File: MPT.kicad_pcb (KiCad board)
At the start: 2 copper layers, 60 x 50 mm, 55 parts, among them J1 USB4105GFA120, J2 ER-TFT2.79-1, Q1 BSS138, SW1 OS102011MA1QN1, SW2 KMR421GULCLFS, SW3 KMR421GULCLFS, U1 TPS62590, U2 BQ25185, U3 BQ27441-G1, U4 ESP32-S3-WROOM-1-N4R2, U5 RCLAMP0854P.TCT

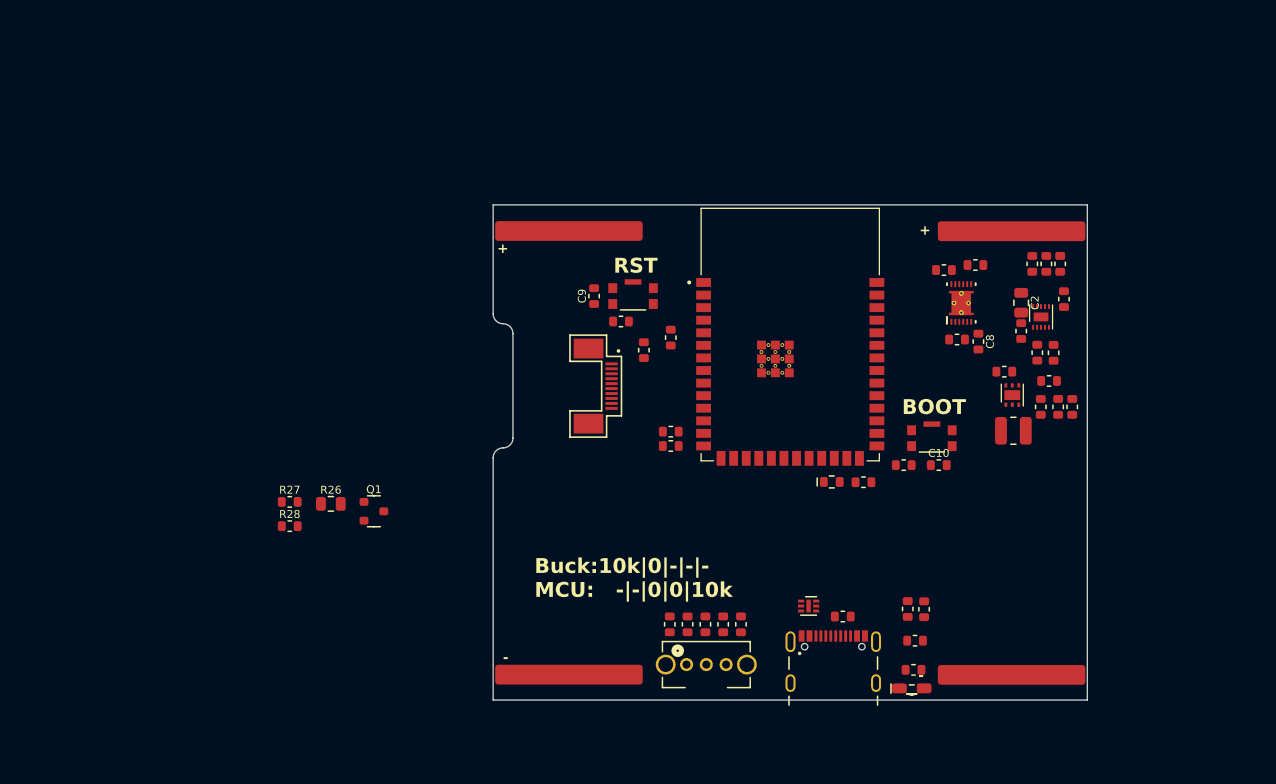
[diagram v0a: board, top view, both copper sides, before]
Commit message: Updated PCB Layout with new Buck Boost, Display driver and STAT Led logic
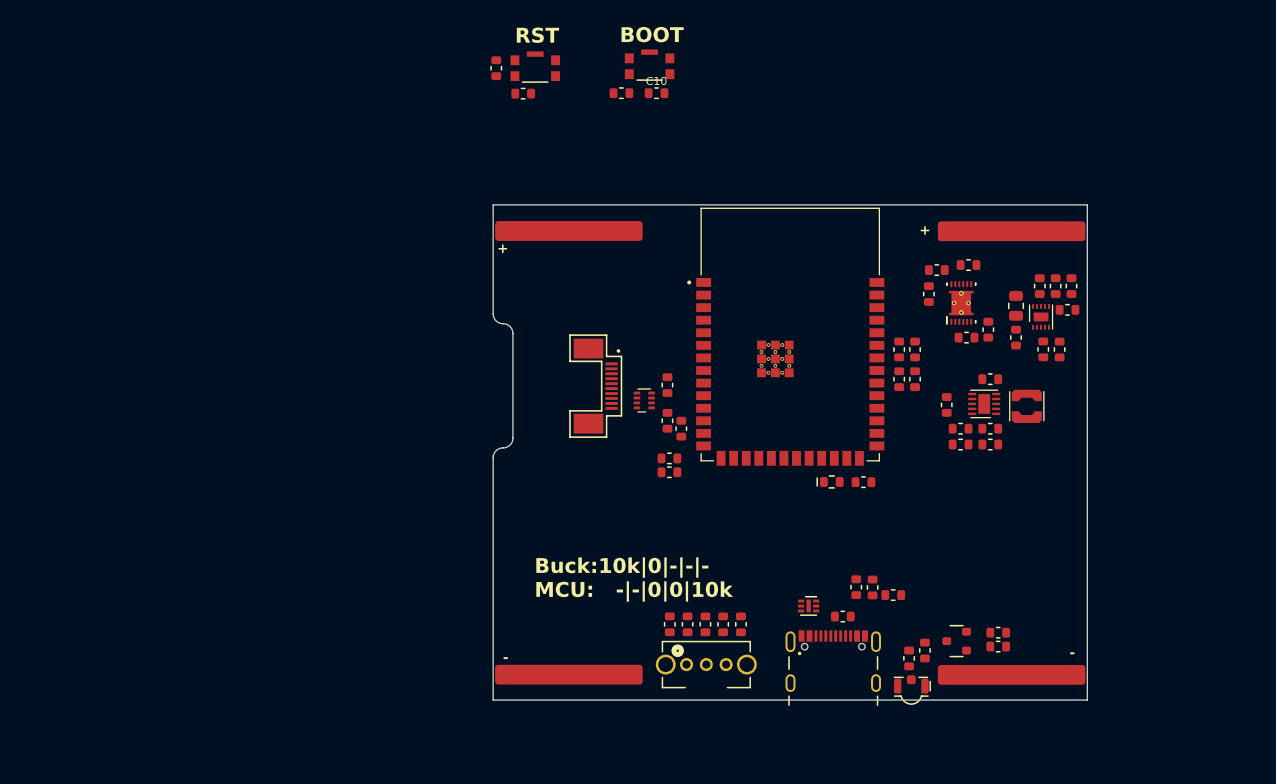
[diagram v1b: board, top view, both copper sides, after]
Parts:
- removed C3: 22p, passive:C_0603
- removed C5: 10u, passive:C_0603
- removed L1: 2u2, passive:L_3.2mmx2.5mm
- removed Q1: BSS138, package:SOT-23
- removed R26: 5R11, passive:R_0805
- removed U1: TPS62590, package:WSON-6-1EP_2x2mm_P0.65mm
- added C11: 10u, passive:C_0603, F.Cu at (177.8, 100.1)
- added C12: 100n, passive:C_0603, F.Cu at (173.4, 102.7)
- added C13: 10u, passive:C_0603, F.Cu at (177.8, 105.1)
- added C14: 10u, passive:C_0603, F.Cu at (177.8, 106.7)
- added L4: 1u5, passive:L_Coilcraft_LPS301X, F.Cu at (181.4, 102.8)
- added Q2: BSS138, package:SOT-23, F.Cu at (174.4, 126.5)
- added R25: 10k, passive:R_0603, F.Cu at (168.6, 97.1)
- added R29: 100k, passive:R_0603, F.Cu at (178.6, 125.7)
- added R30: 100R, passive:R_0603, F.Cu at (178.6, 127.1)
- added R31: 20k, passive:R_0603, F.Cu at (170.2, 97.1)
- added R32: 10k, passive:R_0603, F.Cu at (170.2, 100.1)
- added R33: 20k, passive:R_0603, F.Cu at (168.6, 100.1)
- added U6: TPS63030, package:WSON-10-1EP_2.5x2.5mm_P0.5mm, F.Cu at (177.1, 102.6)
- added U7: LP5816, package:SOT-583, F.Cu at (142.8, 102.2)
- C1: value 10u -> 1u
- D1: value Red -> LTST-S326KGJRKT; footprint diode:LED_0805_Right_Angle -> diode:LED_RG_0805_Right_Angle
- R10: value 619k -> 150R
- R11: value 137k -> 150R
- R20: value 1k -> 100R
- R27: value 100k -> 196k
- R28: value 100R -> 1M15
- moved R28 68.2 mm to (174.8, 106.7)
- moved R27 68.1 mm to (174.8, 105.1), turned to 180 degrees
- moved C10 47.1 mm to (144.1, 71.2)
- moved R17 47.1 mm to (140.5, 71.2)
- moved SW3 47.1 mm to (143.4, 68.5)
- moved R13 38.0 mm to (171.6, 91.5), turned to 90 degrees
- moved C1 34.0 mm to (145.2, 100.7), turned to 90 degrees
- moved R11 30.0 mm to (171.2, 127.5), turned to 90 degrees
- moved R10 29.5 mm to (169.6, 128.3)
- moved C9 25.0 mm to (127.9, 68.7)
- moved R16 25.0 mm to (130.6, 71.2)
- moved SW2 25.0 mm to (131.8, 68.7)
- moved R18 9.26 mm to (146.6, 105.1), turned to 90 degrees
- moved R19 7.52 mm to (145.2, 104.3), turned to 90 degrees
- moved R21 5.65 mm to (165.9, 121.1)
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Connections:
- C1 pad 1: VSYS -> +3V4
- D1 pad 1: Net-(D1-A) -> Net-(D1-C_R)
- D1 pad 2: /BMS/GAUGE_GPOUT -> VBUS_INT
- J2 pad 7: +3V3 -> +3V4
- J2 pad 9: +3V3 -> +3V4
- R1 pad 2: /Buck_En -> /BUCK_EN
- R10 pad 1: +3V3 -> Net-(D1-C_G)
- R10 pad 2: Net-(U1-FB) -> Net-(Q2-D)
- R11 pad 1: Net-(U1-FB) -> Net-(D1-C_R)
- R11 pad 2: GND -> /BMS/STAT2
- R13 pad 1: +3V3 -> +3V4
- R13 pad 2: Net-(D1-A) -> /BMS/GAUGE_GPOUT
- R16 pad 2: +3V3 -> +3V4
- R17 pad 1: +3V3 -> +3V4
- R18 pad 1: +3V3 -> +3V4
- R18 pad 2: /BMS/GAUGE_I2C_SCL -> /BMS/I2C_SCL
- R19 pad 1: +3V3 -> +3V4
- R19 pad 2: /BMS/GAUGE_I2C_SDA -> /BMS/I2C_SDA
- R20 pad 1: +3V3 -> +3V4
- R27 pad 1: Net-(Q1-G) -> Net-(U6-FB)
- R28 pad 1: Net-(Q1-G) -> +3V4
- R28 pad 2: /Display/DISP_BACKLIGHT -> Net-(U6-FB)
- R3 pad 1: /Buck_En -> /BUCK_EN
- R4 pad 1: +3V3 -> +3V4
- R6 pad 1: +3V3 -> VBUS_INT
- R6 pad 2: /BMS/CHRG_STAT2 -> /BMS/STAT2
- R8 pad 1: +3V3 -> VBUS_INT
- R8 pad 2: /BMS/CHRG_STAT1 -> /BMS/STAT1
- U2 pad 3: /BMS/CHRG_STAT2 -> /BMS/STAT2
- U2 pad 9: /BMS/CHRG_STAT1 -> /BMS/STAT1
- U3 pad 1: /BMS/GAUGE_I2C_SDA -> /BMS/I2C_SDA
- U3 pad 2: /BMS/GAUGE_I2C_SCL -> /BMS/I2C_SCL
- U4 pad 10: /MCU/SLEEP_CTRL_PIN -> /Display/SPI2_CS0_DISP
- U4 pad 11: unconnected-(U4-IO18-Pad11) -> /BMS/I2C_SDA
- U4 pad 12: /Display/DISP_BACKLIGHT -> /BMS/I2C_SCL
- U4 pad 17: /Display/SPI2_SCL -> unconnected-(U4-IO9-Pad17)
- U4 pad 18: /Display/SPI2_SDA -> unconnected-(U4-IO10-Pad18)
- U4 pad 19: /Display/SPI2_CS0_DISP -> unconnected-(U4-IO11-Pad19)
- U4 pad 2: +3V3 -> +3V4
- U4 pad 20: /Display/DISP_RS -> unconnected-(U4-IO12-Pad20)
- U4 pad 21: /Display/DISP_RESET -> unconnected-(U4-IO13-Pad21)
- U4 pad 22: unconnected-(U4-IO14-Pad22) -> /MCU/RTC_INT
- U4 pad 32: unconnected-(U4-IO39-Pad32) -> /MCU/SLEEP_CTRL_PIN
- U4 pad 35: /BMS/GAUGE_GPOUT -> unconnected-(U4-IO42-Pad35)
- U4 pad 39: unconnected-(U4-IO1-Pad39) -> /BMS/GAUGE_GPOUT
- U4 pad 4: unconnected-(U4-IO4-Pad4) -> /Display/SPI2_SDA
- U4 pad 5: unconnected-(U4-IO5-Pad5) -> /Display/SPI2_SCL
- U4 pad 6: /BMS/GAUGE_I2C_SCL -> /Display/DISP_RS
- U4 pad 7: /BMS/GAUGE_I2C_SDA -> /Display/DISP_RESET

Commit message: Footprints added, Userbuttons and RTC added on PCB Layout
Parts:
- removed R1, R2, R4: 0, passive:R_0603_DNP
- removed R3: 0, passive:R_0603
- removed R5: 10k, passive:R_0603
- added C15: 1uF, Capacitor_SMD:C_0603_1608Metric, F.Cu at (151.8, 119.9)
- added C16: 1uF, Capacitor_SMD:C_0603_1608Metric, F.Cu at (161.6, 120.1)
- added C18: 1uF, Capacitor_SMD:C_0603_1608Metric, F.Cu at (183.0, 112.5)
- added C19: 1uF, Capacitor_SMD:C_0603_1608Metric, F.Cu at (177.2, 111.3)
- added C20: 1uF, Capacitor_SMD:C_0603_1608Metric, F.Cu at (184.2, 116.1)
- added C21: 1uF, Capacitor_SMD:C_0603_1608Metric, F.Cu at (186.2, 122.1)
- added C22: 1uF, Capacitor_SMD:C_0603_1608Metric, F.Cu at (172.5, 111.2)
- added C3: 1uF, Capacitor_SMD:C_0603_1608Metric, F.Cu at (133.0, 116.7)
- added C5: 1uF, Capacitor_SMD:C_0603_1608Metric, F.Cu at (142.4, 122.9)
- added R26: 10k, Resistor_SMD:R_0603_1608Metric, F.Cu at (134.8, 116.7)
- added R34: 10k, Resistor_SMD:R_0603_1608Metric, F.Cu at (144.0, 122.9)
- added R35: 10k, Resistor_SMD:R_0603_1608Metric, F.Cu at (153.4, 119.9)
- added R36: 10k, Resistor_SMD:R_0603_1608Metric, F.Cu at (163.2, 120.1)
- added R38: 10k, Resistor_SMD:R_0603_1608Metric, F.Cu at (184.6, 112.5)
- added R39: 10k, Resistor_SMD:R_0603_1608Metric, F.Cu at (178.8, 111.3)
- added R40: 10k, Resistor_SMD:R_0603_1608Metric, F.Cu at (185.8, 116.1)
- added R41: 10k, Resistor_SMD:R_0603_1608Metric, F.Cu at (184.6, 122.1)
- added R42: 10k, Resistor_SMD:R_0603_1608Metric, F.Cu at (174.2, 111.2)
- added R43: 4k7, Resistor_SMD:R_0603_1608Metric, F.Cu at (141.1, 108.3)
- added RTC1: RV-8263-C8, RV_8263_C8_32_768KHZ_20PPM_TA_QC:IC_RV-8263-C8-32.768KHZ-20PPM-TA-QC, F.Cu at (137.4, 109.6)
- added S1: 2434804-1, 2434804_1:SW_2434804-1, B.Cu at (176.6, 120.0)
- added SW4: SW_1825910-6, 1825910-6:SW_1825910-6-4, B.Cu at (134.1, 117.0)
- added SW5: SW_1825910-6, 1825910-6:SW_1825910-6-4, B.Cu at (143.1, 123.0)
- added SW6: SW_1825910-6, 1825910-6:SW_1825910-6-4, B.Cu at (152.6, 120.0)
- added SW7: SW_1825910-6, 1825910-6:SW_1825910-6-4, B.Cu at (162.6, 120.0)
- moved R22 4.33 mm to (168.0, 123.3)
- moved R21 4.10 mm to (169.4, 123.3)
- moved L2 3.13 mm to (170.8, 123.3), turned to 90 degrees
- moved U5 2.25 mm to (161.6, 123.7)
- moved L3 1.89 mm to (164.8, 124.1)
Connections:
- R23 pad 2: /MCU/USB_DM -> /MCU/USB_DP
- R24 pad 1: /MCU/USB_DP -> /MCU/USB_DM
- U4 pad 17: unconnected-(U4-IO9-Pad17) -> /MCU/GPIO_JOYSTICK_UP
- U4 pad 18: unconnected-(U4-IO10-Pad18) -> /MCU/GPIO_JOYSTICK_RIGHT
- U4 pad 19: unconnected-(U4-IO11-Pad19) -> /MCU/GPIO_JOYSTICK_CENTER
- U4 pad 20: unconnected-(U4-IO12-Pad20) -> /MCU/GPIO_JOYSTICK_LEFT
- U4 pad 21: unconnected-(U4-IO13-Pad21) -> /MCU/GPIO_JOYSTICK_DOWN
- U4 pad 24: unconnected-(U4-IO47-Pad24) -> /MCU/GPIO_BUTTON4
- U4 pad 25: unconnected-(U4-IO48-Pad25) -> /MCU/GPIO_BUTTON5
- U4 pad 31: unconnected-(U4-IO38-Pad31) -> /MCU/GPIO_BUTTON2
- U4 pad 35: unconnected-(U4-IO42-Pad35) -> /MCU/GPIO_BUTTON3
- U4 pad 38: unconnected-(U4-IO2-Pad38) -> /MCU/GPIO_BUTTON1
- U6 pad 6: /BUCK_EN -> /BMS/BUCK_EN

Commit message: Started routing of componentes
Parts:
- added R1: 0, passive:R_0603_DNP, F.Cu at (134.2, 121.1)
- added R2: 0, passive:R_0603_DNP, F.Cu at (134.2, 124.3)
- added R3: 0, passive:R_0603, F.Cu at (134.2, 122.7)
- added R4: 0, passive:R_0603_DNP, F.Cu at (134.2, 125.9)
- added R5: 10k, passive:R_0603, F.Cu at (134.2, 127.5)
- L4: footprint passive:L_Coilcraft_LPS301X -> passive:L_2.5mmx1.9mm
- moved C10 22.8 mm to (144.2, 94.0)
- moved R17 22.8 mm to (140.6, 94.0)
- moved SW3 22.8 mm to (143.5, 91.3)
- moved C9 22.7 mm to (131.1, 91.2)
- moved R16 22.7 mm to (133.8, 93.7)
- moved SW2 22.7 mm to (135.1, 91.2)
- moved L2 16.4 mm to (155.8, 129.9)
- moved R22 12.7 mm to (155.6, 126.1)
- moved R8 5.91 mm to (180.4, 90.3)
- moved R21 4.81 mm to (168.0, 127.9)
- moved L3 4.24 mm to (169.0, 123.5)
- moved R23 3.49 mm to (144.6, 111.5), turned to 90 degrees
- moved R18 1.97 mm to (144.8, 105.9)
- moved R19 1.97 mm to (143.4, 105.1)
- moved C8 1.60 mm to (177.7, 93.5)
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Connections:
- U4 pad 10: /Display/SPI2_CS0_DISP -> /BMS/I2C_SCL
- U4 pad 11: /BMS/I2C_SDA -> unconnected-(U4-IO18-Pad11)
- U4 pad 12: /BMS/I2C_SCL -> unconnected-(U4-IO8-Pad12)
- U4 pad 24: /MCU/GPIO_BUTTON4 -> unconnected-(U4-IO47-Pad24)
- U4 pad 25: /MCU/GPIO_BUTTON5 -> unconnected-(U4-IO48-Pad25)
- U4 pad 32: /MCU/SLEEP_CTRL_PIN -> /MCU/GPIO_BUTTON3
- U4 pad 33: /BMS/CHRG_STAT1 -> /MCU/GPIO_BUTTON4
- U4 pad 34: /BMS/CHRG_STAT2 -> /BMS/CHRG_STAT1
- U4 pad 35: /MCU/GPIO_BUTTON3 -> /BMS/CHRG_STAT2
- U4 pad 8: unconnected-(U4-IO15-Pad8) -> /Display/SPI2_CS0_DISP
- U4 pad 9: unconnected-(U4-IO16-Pad9) -> /BMS/I2C_SDA
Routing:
- net /BMS/BUCK_EN: track 0.00 -> 111.1 mm, vias 0 -> 2
- net +BATT: track 0.00 -> 61.8 mm, vias 0 -> 6
- net VBUS_INT: track 0.00 -> 56.4 mm, vias 0 -> 2
- net /BMS/I2C_SCL: track 0.00 -> 39.3 mm, vias 0 -> 2
- net /BMS/I2C_SDA: track 0.00 -> 38.2 mm, vias 0 -> 2
- net Net-(J1-DP1): track 0.00 -> 34.2 mm, vias 0 -> 2
- net Net-(J1-DN1): track 0.00 -> 33.5 mm, vias 0 -> 2
- net /MCU/Boot Mode: track 0.00 -> 32.5 mm, vias 0 -> 2
- net /MCU/Chip Enable/Reset: track 0.00 -> 22.8 mm
- net SHELL_GND: track 0.00 -> 18.9 mm
- net Net-(SW1-B): track 0.00 -> 17.6 mm
- net VBAT: track 0.00 -> 17.4 mm, vias 0 -> 2
- net VBUS_EXT: track 0.00 -> 15.8 mm
- net Net-(SW1-A): track 0.00 -> 14.3 mm
- net /Display/SPI2_SDA: track 0.00 -> 11.1 mm
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
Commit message: Mountingholes Added
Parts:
- added H1: MountingHole, MountingHole:MountingHole_2.2mm_M2, F.Cu at (145.4, 85.3)
- added H2: MountingHole, MountingHole:MountingHole_2.2mm_M2, F.Cu at (130.2, 125.3)
- added H3: MountingHole, MountingHole:MountingHole_2.2mm_M2, F.Cu at (182.8, 125.9)
- added H4: MountingHole, MountingHole:MountingHole_2.2mm_M2, F.Cu at (169.8, 85.3)
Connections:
- U4 pad 24: unconnected-(U4-IO47-Pad24) -> /MCU/SLEEP_CTRL_PIN

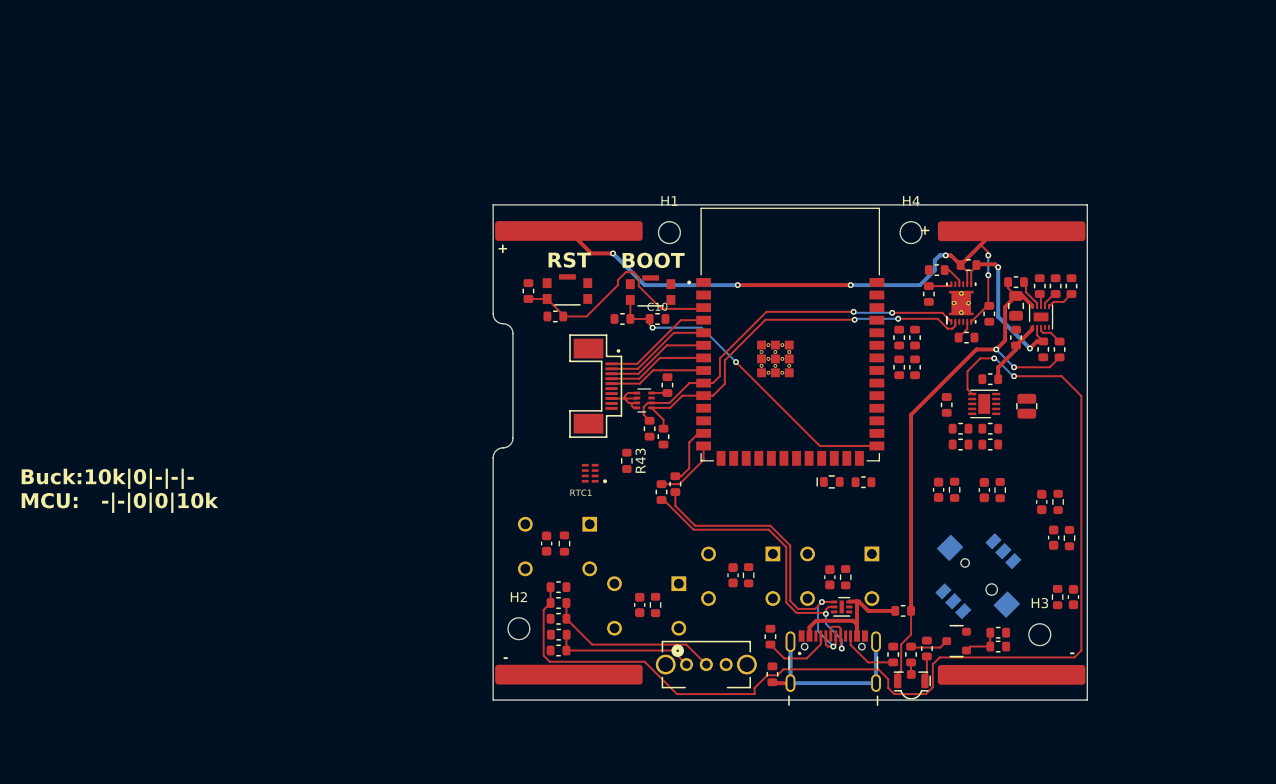
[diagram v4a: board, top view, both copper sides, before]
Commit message: Replace LED Driver Remove maybe buzzer
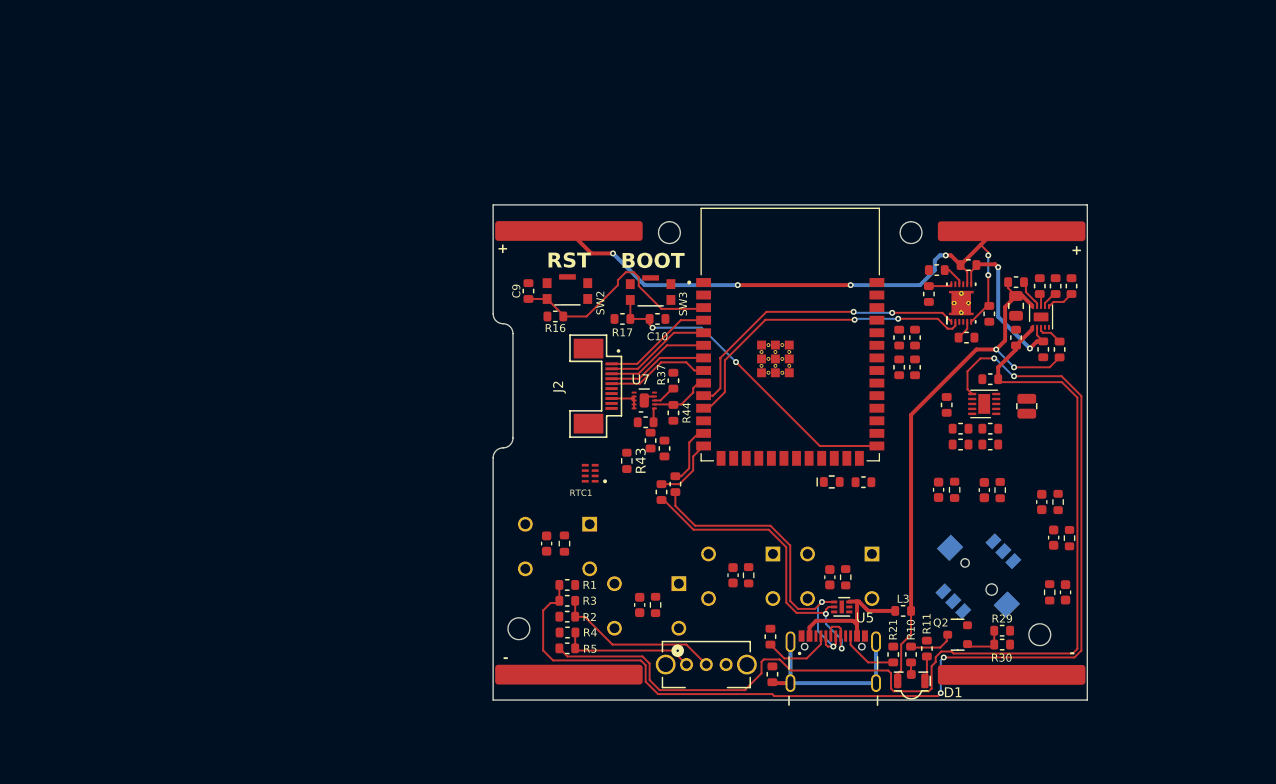
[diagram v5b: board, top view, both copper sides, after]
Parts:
- added R37: 18k2, passive:R_0603, F.Cu at (145.8, 100.2)
- added R44: 200k, passive:R_0603, F.Cu at (145.8, 103.5)
- U7: value LP5816 -> MIC2841A; footprint package:SOT-583 -> package:MLF-10_MT_MCH
- moved C1 4.35 mm to (143.0, 104.4), turned to 180 degrees
- moved R18 1.20 mm to (144.9, 107.1)
- moved R19 1.20 mm to (143.5, 106.3)
- moved C21 0.93 mm to (185.4, 121.6)
- moved R41 0.93 mm to (183.8, 121.6)
- moved R2 0.91 mm to (135.0, 124.0)
- moved R3 0.91 mm to (135.0, 122.4)
- moved R5 0.91 mm to (135.0, 127.2)
- moved R1 0.91 mm to (135.0, 120.8)
- moved R4 0.91 mm to (135.1, 125.6)
- moved Q2 0.66 mm to (174.5, 125.9)
- moved R29 0.45 mm to (179.0, 125.5)
- moved R30 0.45 mm to (179.0, 126.9)
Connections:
- R18 pad 2: /BMS/I2C_SCL -> /BMS/I2C_SDA
- R19 pad 2: /BMS/I2C_SDA -> /BMS/I2C_SCL
- U4 pad 10: /BMS/I2C_SCL -> /BMS/I2C_SDA
- U4 pad 11: unconnected-(U4-IO18-Pad11) -> /BMS/I2C_SCL
- U4 pad 12: unconnected-(U4-IO8-Pad12) -> /MCU/SLEEP_CTRL_PIN
- U4 pad 24: /MCU/SLEEP_CTRL_PIN -> unconnected-(U4-IO47-Pad24)
- U4 pad 9: /BMS/I2C_SDA -> /Display/BACKLIGHT_PWM
- U7 pad 1: /BMS/I2C_SCL -> +3V4
- U7 pad 2: /BMS/I2C_SDA -> /Display/BACKLIGHT_PWM
- U7 pad 3: GND -> Net-(U7-RSET)
- U7 pad 4: +3V4 -> GND
- U7 pad 5: Net-(J2-LEDK) -> unconnected-(U7-NC-Pad5)
- U7 pad 6: Net-(J2-LEDK) -> unconnected-(U7-NC-Pad6)
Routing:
- net VSYS: track 6.65 -> 103.7 mm
- net /BMS/I2C_SDA: track 38.2 -> 30.8 mm
- net /BMS/I2C_SCL: track 39.3 -> 32.0 mm
- net /Display/BACKLIGHT_PWM: track 0.00 -> 6.11 mm
- net Net-(J2-LEDK): track 6.53 -> 3.84 mm
- net Net-(U7-RSET): track 0.00 -> 2.41 mm
- net GND: track 0.00 -> 1.19 mm
- net Net-(SW1-A): track 14.3 -> 13.5 mm
- net Net-(SW1-B): track 17.6 -> 16.8 mm
- net Net-(Q2-D): track 3.91 -> 4.60 mm
- net /Display/SPI2_CS0_DISP: track 9.86 -> 10.5 mm
- net /BMS/BUCK_EN: track 111.1 -> 110.6 mm, vias 2 -> 4
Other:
- board text removed: "Buck:10k|0|-|-|- MCU: -|-|0|0|10k"
